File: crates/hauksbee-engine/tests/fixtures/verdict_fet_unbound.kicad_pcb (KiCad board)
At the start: 3 parts, among them Q1 XFET9999

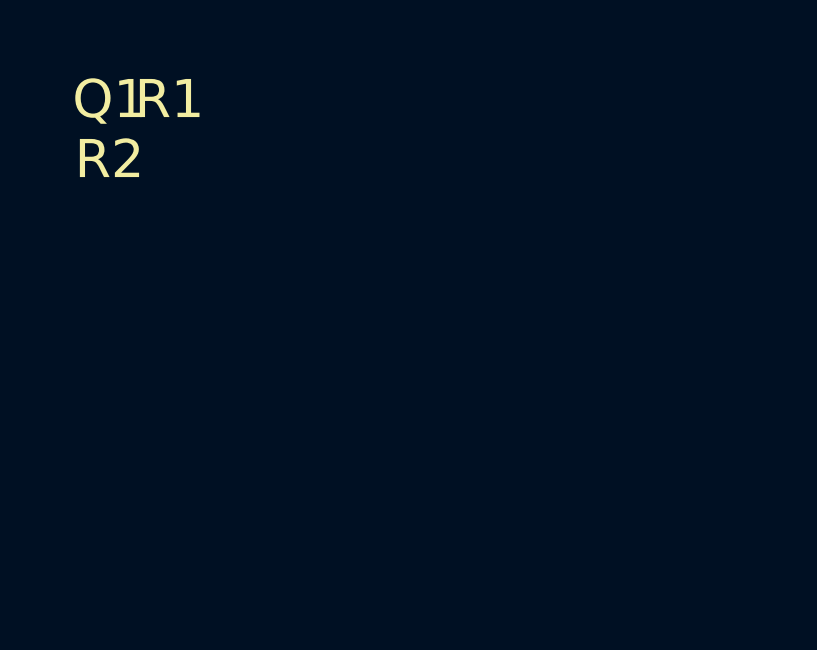
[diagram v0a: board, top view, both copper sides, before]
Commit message: Fix verdict fixtures and thermal JSON path; regenerate run-report schema; unify AC caveat prefix
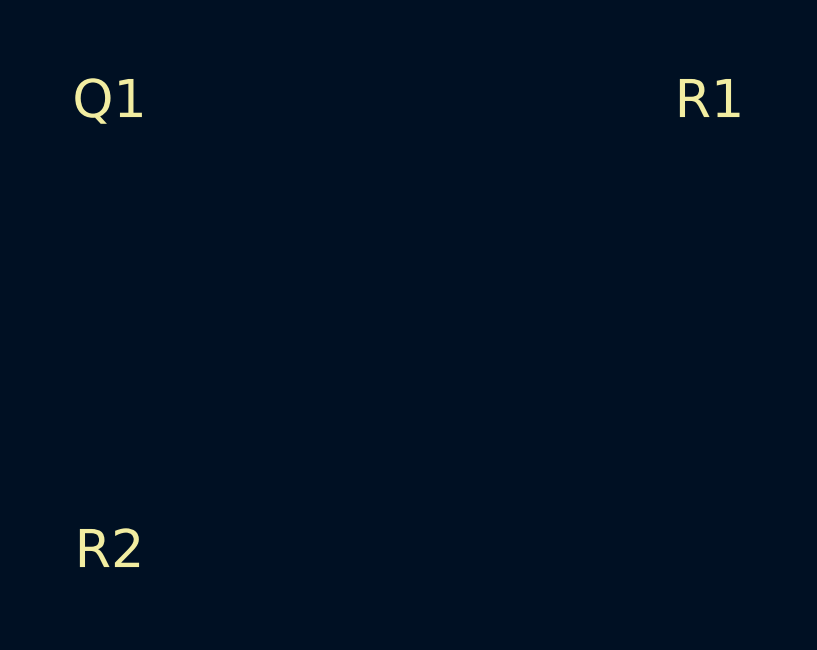
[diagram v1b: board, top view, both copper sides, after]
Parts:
- moved R1 18.0 mm to (130.0, 100.0)
- moved R2 13.0 mm to (110.0, 115.0)
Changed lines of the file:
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@@
   )
   (module Resistor_THT:R_Axial_DIN0207_L6.3mm_D2.5mm (layer F.Cu)
-    (at 112 100)
+    (at 130 100)
     (fp_text reference R1 (at 0 0) (layer F.SilkS))
     (fp_text value 1k (at 0 2) (layer F.Fab))
@@
   )
   (module Resistor_THT:R_Axial_DIN0207_L6.3mm_D2.5mm (layer F.Cu)
-    (at 110 102)
+    (at 110 115)
     (fp_text reference R2 (at 0 0) (layer F.SilkS))
     (fp_text value 10k (at 0 2) (layer F.Fab))
